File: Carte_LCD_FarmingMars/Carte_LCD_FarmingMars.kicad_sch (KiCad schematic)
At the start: 21 parts, among them J2 Conn_01x02_Pin, J3 Conn_01x04_Pin, J4 Conn_01x02_Pin, SW1 SW_DIP_x01, SW2 SW_Push, SW3 SW_Push, U1 3V3 reg, U2 ATtiny1616-S

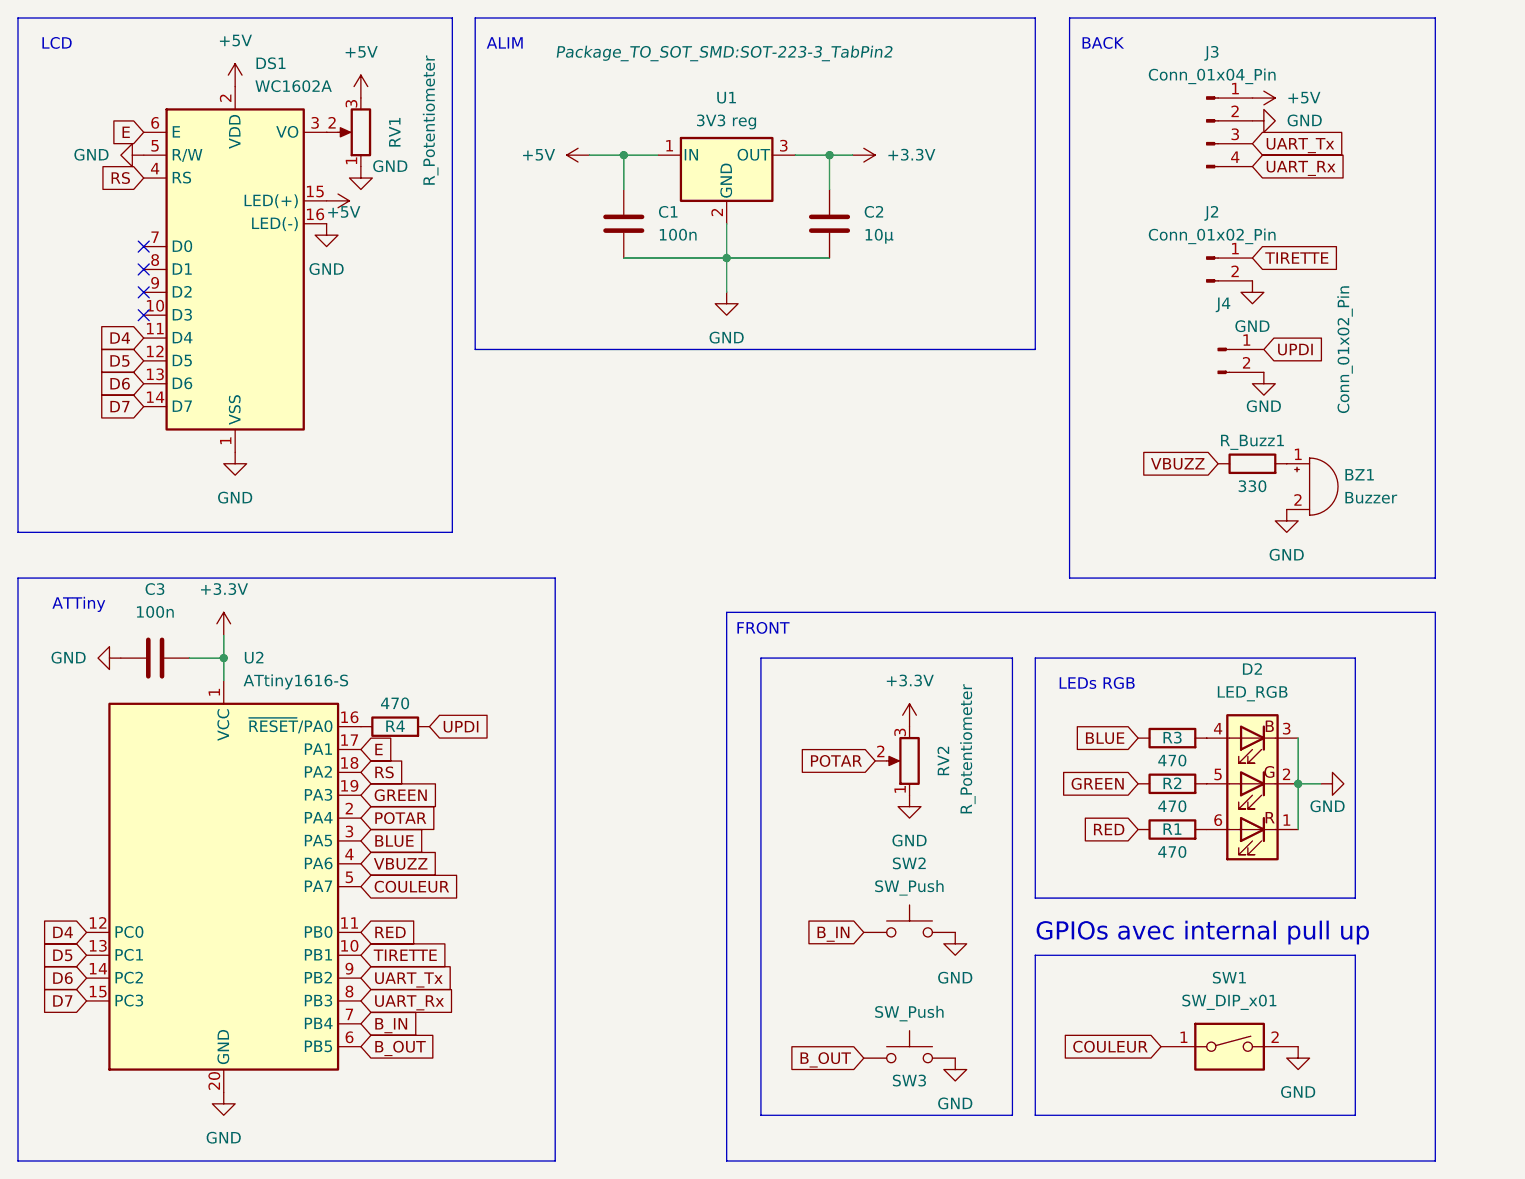
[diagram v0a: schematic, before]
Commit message: trou + bug footprints
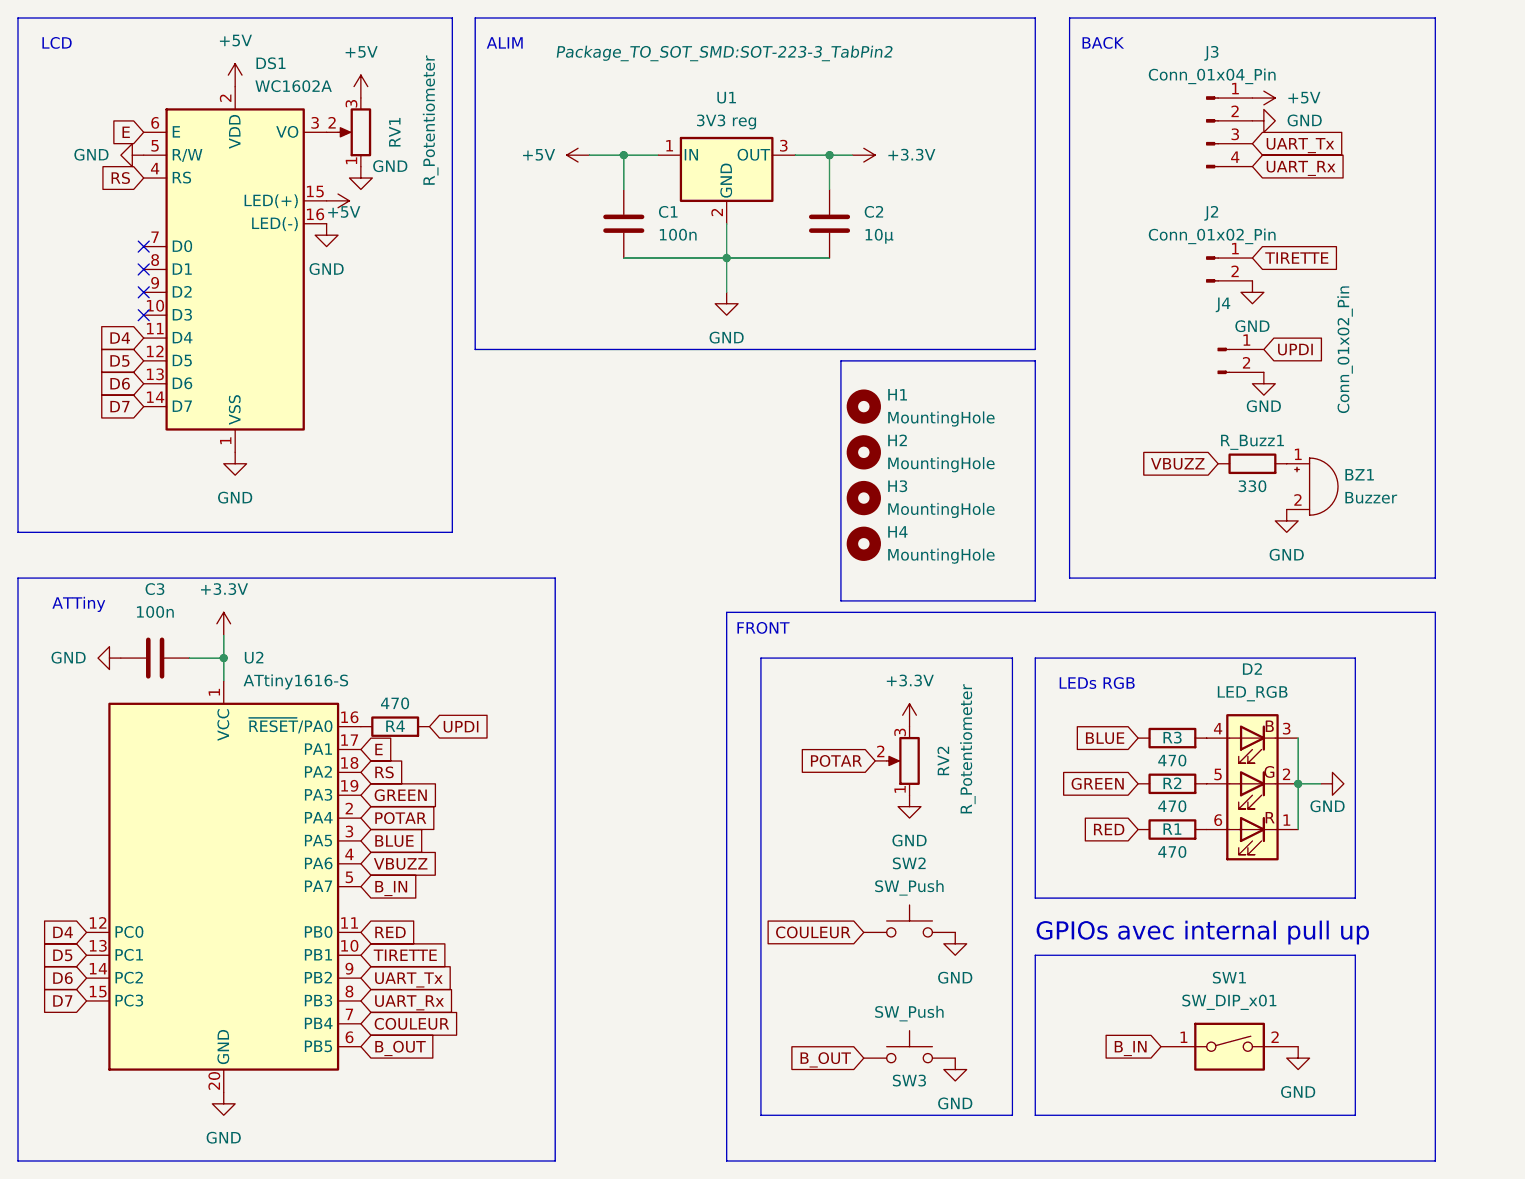
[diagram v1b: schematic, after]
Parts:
- added H1, H2, H3, H4: MountingHole, MountingHole:MountingHole_3.2mm_M3, symbol Mechanical:MountingHole
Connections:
- net B_IN: now also SW1.1, U2.5 (PA7); no longer SW2.1, U2.7 (PB4)
- net COULEUR: now also SW2.1, U2.7 (PB4); no longer SW1.1, U2.5 (PA7)
